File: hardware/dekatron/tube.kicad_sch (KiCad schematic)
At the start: 43 parts, among them J201 TUBE_ANODE, J202 TUBE_A, J203 TUBE_B, Q201 MMBTA42, Q202 MMBTA42, Q203 MMBTA92

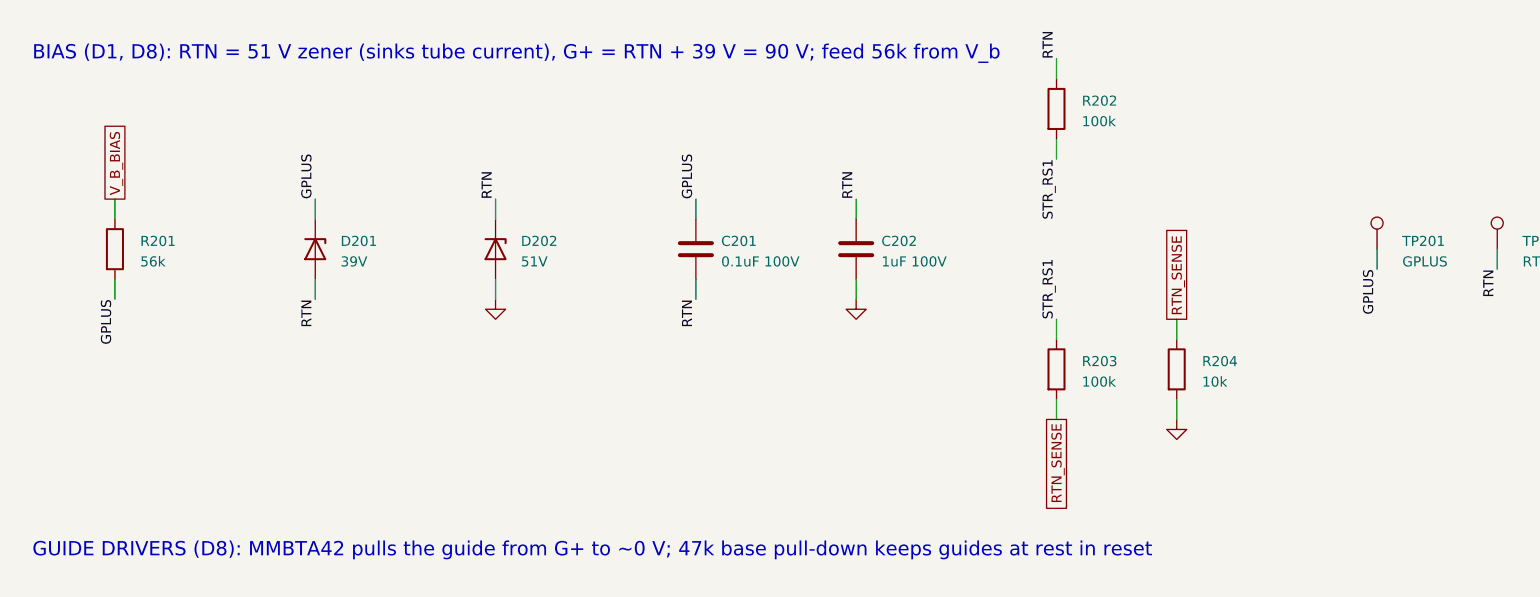
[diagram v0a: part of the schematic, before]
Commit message: Stiffen the G+/RTN feed to 2 x 20k after checking the zener knee current
The MMSZ52xx datasheet gives a 0.5 mA knee, not the 0.25 mA assumed; with
the 56k feed the 51 V zener fell to 0.45 mA at V_b 150 V (RTN_SENSE also
draws 0.24 mA). With 2 x 20k it stays >= 0.87 mA; RTN 51.1-51.4 V across
corners. Zener models now use datasheet I_ZT/Z_ZT. V_b load budget
updated (~4.7 mA).

Co-Authored-By: Claude Opus 5.5 <noreply@anthropic.com>
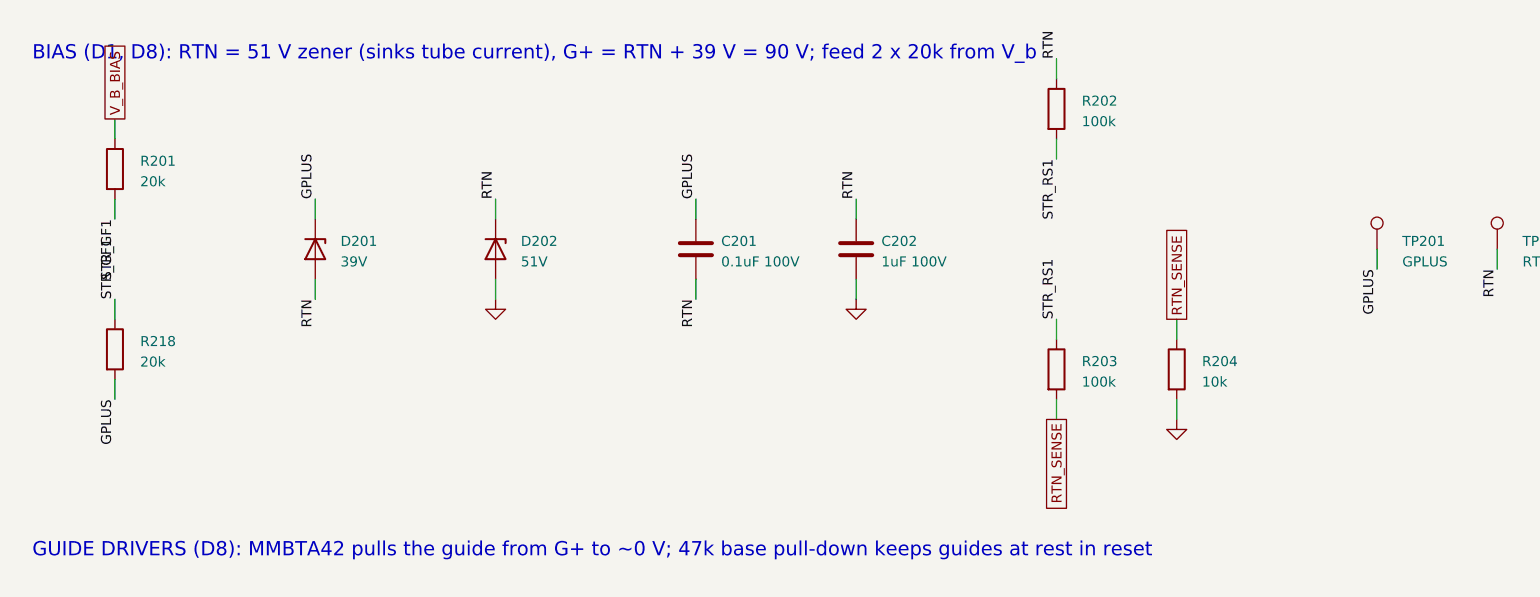
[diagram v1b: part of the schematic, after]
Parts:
- added R218: 20k, Resistor_SMD:R_1206_3216Metric, symbol Device:R
- R201: value 56k -> 20k; Function G+ / RTN feed (1.2 mA at V_b 157 V) -> G+ / RTN feed 1/2 (2 x 20k: 1.5-2.1 mA)
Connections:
- net GPLUS: now also R218.2; no longer R201.2
- new net STR_GF1: R201.2, R218.1
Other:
- note added: "BIAS (D1, D8): RTN = 51 V zener (sinks tube current), G+ = RTN + 39 V = 90 V; feed 2 x 20k from V_b"
- note removed: "BIAS (D1, D8): RTN = 51 V zener (sinks tube current), G+ = RTN + 39 V = 90 V; feed 56k from V_b"
- moved on the sheet: R201
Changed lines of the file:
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@@
 	(paper "A3")
 	(title_block (title "Tube: G+ / RTN bias, guide drivers, index sense, anode, harness") (rev "Rev A draft") (company "universal-nixie-display (open hardware)") (comment 1 "Generated by tools/gen_schematics.py; values per docs/hardware.md"))
-	(text "BIAS (D1, D8): RTN = 51 V zener (sinks tube current), G+ = RTN + 39 V = 90 V; feed 56k from V_b" (exclude_from_sim no) (at 20 22 0) (effects (font (size 1.8 1.8)) (justify left bottom)))
-	(symbol (lib_id "Device:R") (at 30.48 45.72 0) (unit 1) (body_style 1) (exclude_from_sim no) (in_bom yes) (on_board yes) (in_pos_files yes) (dnp no)
-	  (property "Reference" "R201" (at 33.68 44.72 0) (show_name no) (do_not_autoplace no) (effects (font (size 1.27 1.27)) (justify left)))
-	  (property "Value" "56k" (at 33.68 47.32 0) (show_name no) (do_not_autoplace no) (effects (font (size 1.27 1.27)) (justify left)))
-	  (property "Footprint" "Resistor_SMD:R_1206_3216Metric" (at 30.48 45.72 0) (hide yes) (show_name no) (do_not_autoplace no) (effects (font (size 1.27 1.27)) (justify left)))
-	  (property "Datasheet" "" (at 30.48 45.72 0) (hide yes) (show_name no) (do_not_autoplace no) (effects (font (size 1.27 1.27)) (justify left)))
-	  (property "Description" "Resistor" (at 30.48 45.72 0) (hide yes) (show_name no) (do_not_autoplace no) (effects (font (size 1.27 1.27)) (justify left)))
-	  (property "Function" "G+ / RTN feed (1.2 mA at V_b 157 V)" (at 30.48 45.72 0) (hide yes) (show_name no) (do_not_autoplace no) (effects (font (size 1.27 1.27)) (justify left)))
+	(text "BIAS (D1, D8): RTN = 51 V zener (sinks tube current), G+ = RTN + 39 V = 90 V; feed 2 x 20k from V_b" (exclude_from_sim no) (at 20 22 0) (effects (font (size 1.8 1.8)) (justify left bottom)))
+	(symbol (lib_id "Device:R") (at 30.48 35.56 0) (unit 1) (body_style 1) (exclude_from_sim no) (in_bom yes) (on_board yes) (in_pos_files yes) (dnp no)
+	  (property "Reference" "R201" (at 33.68 34.56 0) (show_name no) (do_not_autoplace no) (effects (font (size 1.27 1.27)) (justify left)))
+	  (property "Value" "20k" (at 33.68 37.16 0) (show_name no) (do_not_autoplace no) (effects (font (size 1.27 1.27)) (justify left)))
+	  (property "Footprint" "Resistor_SMD:R_1206_3216Metric" (at 30.48 35.56 0) (hide yes) (show_name no) (do_not_autoplace no) (effects (font (size 1.27 1.27)) (justify left)))
+	  (property "Datasheet" "" (at 30.48 35.56 0) (hide yes) (show_name no) (do_not_autoplace no) (effects (font (size 1.27 1.27)) (justify left)))
+	  (property "Description" "Resistor" (at 30.48 35.56 0) (hide yes) (show_name no) (do_not_autoplace no) (effects (font (size 1.27 1.27)) (justify left)))
+	  (property "Function" "G+ / RTN feed 1/2 (2 x 20k: 1.5-2.1 mA)" (at 30.48 35.56 0) (hide yes) (show_name no) (do_not_autoplace no) (effects (font (size 1.27 1.27)) (justify left)))
 	  (pin "1")
 	  (pin "2")
 	  (instances (project "dekatron" (path "/b14ce2c4-03a1-5284-8a98-bc460407f799/2f366097-8856-550c-8e15-80a7dd2c4e55" (reference "R201") (unit 1))))
 	)
-	(wire (pts (xy 30.48 41.91) (xy 30.48 39.37)) (stroke (width 0) (type default)))
-	(global_label "V_B_BIAS" (shape passive) (at 30.48 39.37 90) (fields_autoplaced yes) (effects (font (size 1.27 1.27)) (justify left)) (property "Intersheetrefs" "${INTERSHEET_REFS}" (at 30.48 39.37 0) (effects (font (size 1.27 1.27)) (hide yes))))
-	(wire (pts (xy 30.48 49.53) (xy 30.48 52.07)) (stroke (width 0) (type default)))
-	(label "GPLUS" (at 30.48 52.07 270) (effects (font (size 1.27 1.27)) (justify right bottom)))
+	(wire (pts (xy 30.48 31.75) (xy 30.48 29.21)) (stroke (width 0) (type default)))
+	(global_label "V_B_BIAS" (shape passive) (at 30.48 29.21 90) (fields_autoplaced yes) (effects (font (size 1.27 1.27)) (justify left)) (property "Intersheetrefs" "${INTERSHEET_REFS}" (at 30.48 29.21 0) (effects (font (size 1.27 1.27)) (hide yes))))
+	(wire (pts (xy 30.48 39.37) (xy 30.48 41.91)) (stroke (width 0) (type default)))
+	(label "STR_GF1" (at 30.48 41.91 270) (effects (font (size 1.27 1.27)) (justify right bottom)))
+	(symbol (lib_id "Device:R") (at 30.48 58.42 0) (unit 1) (body_style 1) (exclude_from_sim no) (in_bom yes) (on_board yes) (in_pos_files yes) (dnp no)
+	  (property "Reference" "R218" (at 33.68 57.42 0) (show_name no) (do_not_autoplace no) (effects (font (size 1.27 1.27)) (justify left)))
+	  (property "Value" "20k" (at 33.68 60.02 0) (show_name no) (do_not_autoplace no) (effects (font (size 1.27 1.27)) (justify left)))
+	  (property "Footprint" "Resistor_SMD:R_1206_3216Metric" (at 30.48 58.42 0) (hide yes) (show_name no) (do_not_autoplace no) (effects (font (size 1.27 1.27)) (justify left)))
+	  (property "Datasheet" "" (at 30.48 58.42 0) (hide yes) (show_name no) (do_not_autoplace no) (effects (font (size 1.27 1.27)) (justify left)))
+	  (property "Description" "Resistor" (at 30.48 58.42 0) (hide yes) (show_name no) (do_not_autoplace no) (effects (font (size 1.27 1.27)) (justify left)))
+	  (property "Function" "G+ / RTN feed 2/2 (<= 93 mW per part at V_b 175 V)" (at 30.48 58.42 0) (hide yes) (show_name no) (do_not_autoplace no) (effects (font (size 1.27 1.27)) (justify left)))
+	  (pin "1")
+	  (pin "2")
+	  (instances (project "dekatron" (path "/b14ce2c4-03a1-5284-8a98-bc460407f799/2f366097-8856-550c-8e15-80a7dd2c4e55" (reference "R218") (unit 1))))
+	)
+	(wire (pts (xy 30.48 54.61) (xy 30.48 52.07)) (stroke (width 0) (type default)))
+	(label "STR_GF1" (at 30.48 52.07 90) (effects (font (size 1.27 1.27)) (justify left bottom)))
+	(wire (pts (xy 30.48 62.23) (xy 30.48 64.77)) (stroke (width 0) (type default)))
+	(label "GPLUS" (at 30.48 64.77 270) (effects (font (size 1.27 1.27)) (justify right bottom)))
 	(symbol (lib_id "Device:D_Zener") (at 55.88 45.72 270) (unit 1) (body_style 1) (exclude_from_sim no) (in_bom yes) (on_board yes) (in_pos_files yes) (dnp no)
 	  (property "Reference" "D201" (at 59.08 44.72 90) (show_name no) (do_not_autoplace no) (effects (font (size 1.27 1.27)) (justify left)))

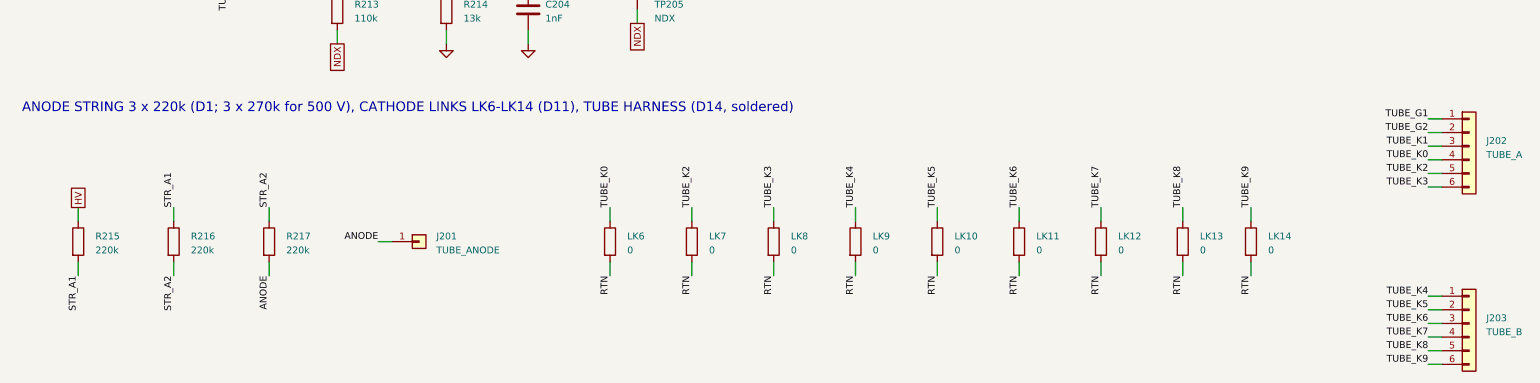
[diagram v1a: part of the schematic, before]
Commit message: Tie the dekatron cathodes at the socket; add Phase 1C PCB tooling (WIP)
Cathodes K0, K2-K9 are joined at the socket and return on one RTN wire, as
in the AD01 reference: LK6-LK14 and J203 removed, tube harness is anode
(J201) + G1, G2, K1, RTN (J202, 4 pads). Netlist diff: only the nine
TUBE_Kn nets and the RTN link pins change. ERC 1 (intentional).

Also adds work-in-progress PCB tooling: gen_pcb.py (pcbnew placement,
outline, pours, rules), route_pcb.py (class-aware A* router adapted from
nanovolt-divider), pcb_io.py, and dekatron.kicad_dru with the corrected
HV pair rules (HV to HV/VB/HVSTR 1.5 mm, to bias/logic 3.0 mm). Harness
landings use plain wire pads with cable-tie anchors. The board itself is
not committed yet: placement is being reworked.

Co-Authored-By: Claude Opus 5.5 <noreply@anthropic.com>
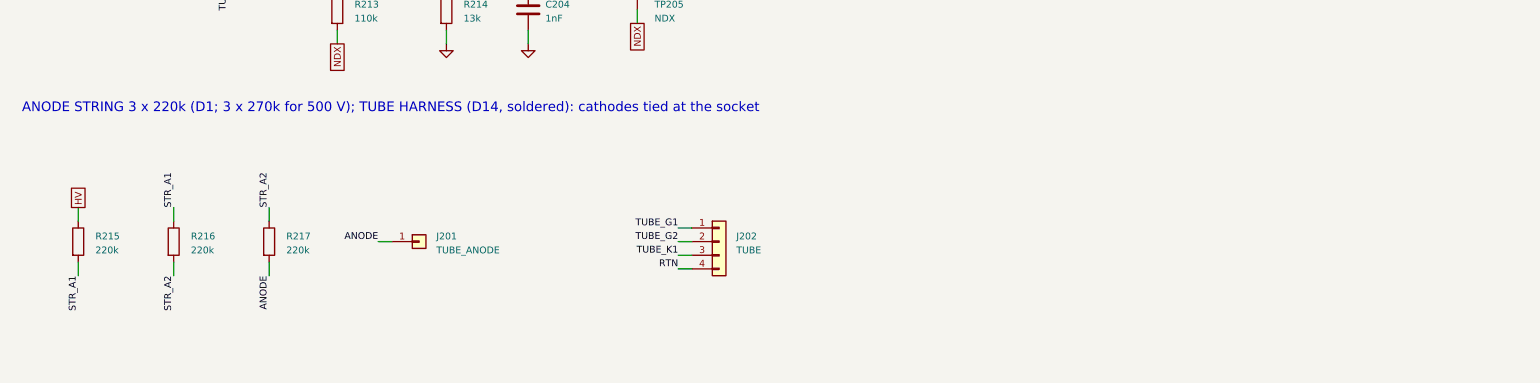
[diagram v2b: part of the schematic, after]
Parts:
- removed J202: TUBE_A, Connector_Wire:SolderWire-0.5sqmm_1x06_P4.8mm_D0.9mm_OD2.3mm_Relief, symbol Connector_Generic:Conn_01x06
- removed J203: TUBE_B, Connector_Wire:SolderWire-0.5sqmm_1x06_P4.8mm_D0.9mm_OD2.3mm_Relief, symbol Connector_Generic:Conn_01x06
- removed LK10, LK11, LK12, LK13, LK14, LK6, LK7, LK8, LK9: 0, Resistor_SMD:R_1206_3216Metric, symbol Device:R
- added J202: TUBE, Connector_Wire:SolderWire-0.5sqmm_1x04_P4.8mm_D0.9mm_OD2.3mm, symbol Connector_Generic:Conn_01x04
- J201: footprint Connector_Wire:SolderWire-0.5sqmm_1x01_D0.9mm_OD2.3mm_Relief -> Connector_Wire:SolderWire-0.5sqmm_1x01_D0.9mm_OD2.3mm
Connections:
- net RTN: now also J202.4 (Pin_4)
- net TUBE_G1: now also J202.1 (Pin_1)
- net TUBE_G2: now also J202.2 (Pin_2)
- net TUBE_K1: now also J202.3 (Pin_3)
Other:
- note added: "ANODE STRING 3 x 220k (D1; 3 x 270k for 500 V); TUBE HARNESS (D14, soldered): cathodes tied at the socket"
- note removed: "ANODE STRING 3 x 220k (D1; 3 x 270k for 500 V), CATHODE LINKS LK6-LK14 (D11), TUBE HARNESS (D14, soldered)"
